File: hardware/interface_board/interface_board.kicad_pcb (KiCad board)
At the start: 2 copper layers, 394.2 x 72.6 mm, 15 parts, among them J1 Conn_01x18_Socket, J10 Conn_01x18_Socket, J2 Conn_01x18_Socket, J3 Conn_01x18_Socket, J4 Conn_01x18_Socket, J5 Conn_01x18_Socket, J6 Conn_01x18_Socket, J7 Conn_01x18_Socket, J8 Conn_01x18_Socket, J9 Conn_01x18_Socket

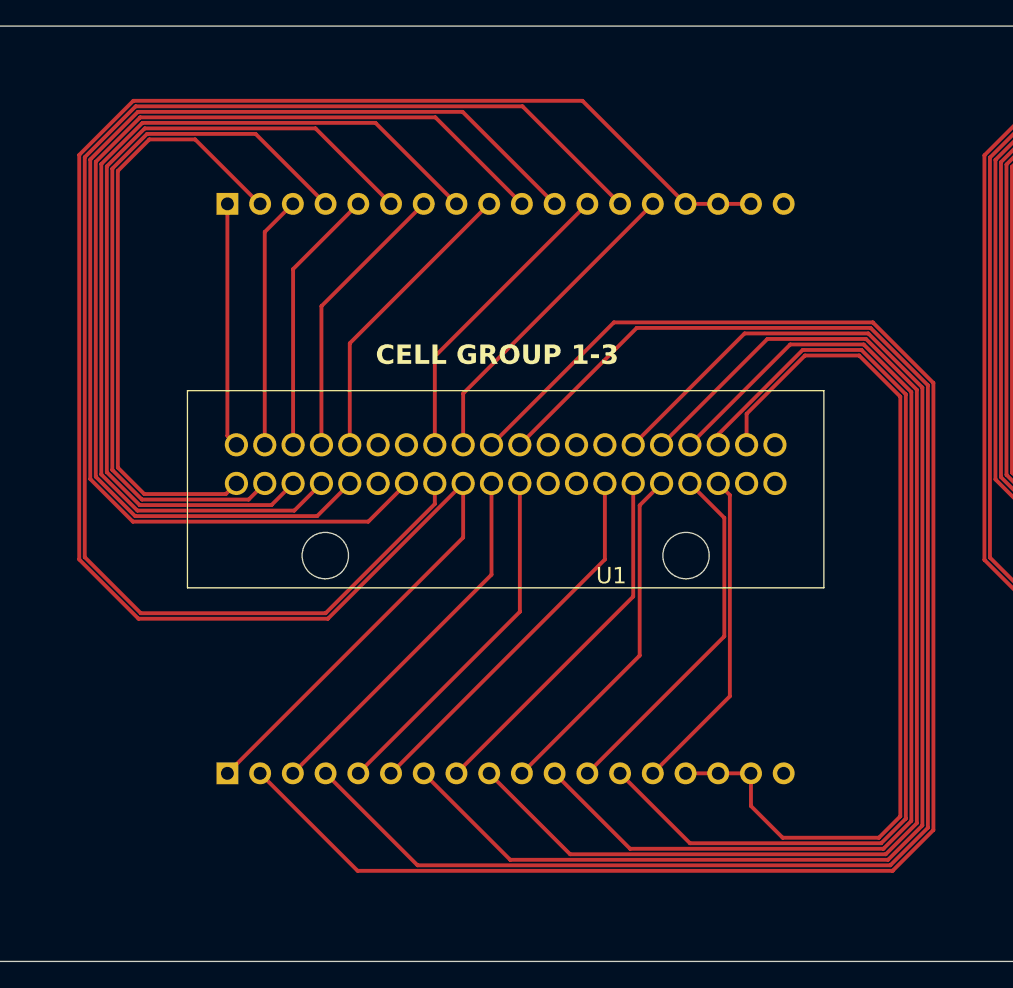
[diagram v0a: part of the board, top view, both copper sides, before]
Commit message: fixed a single connector
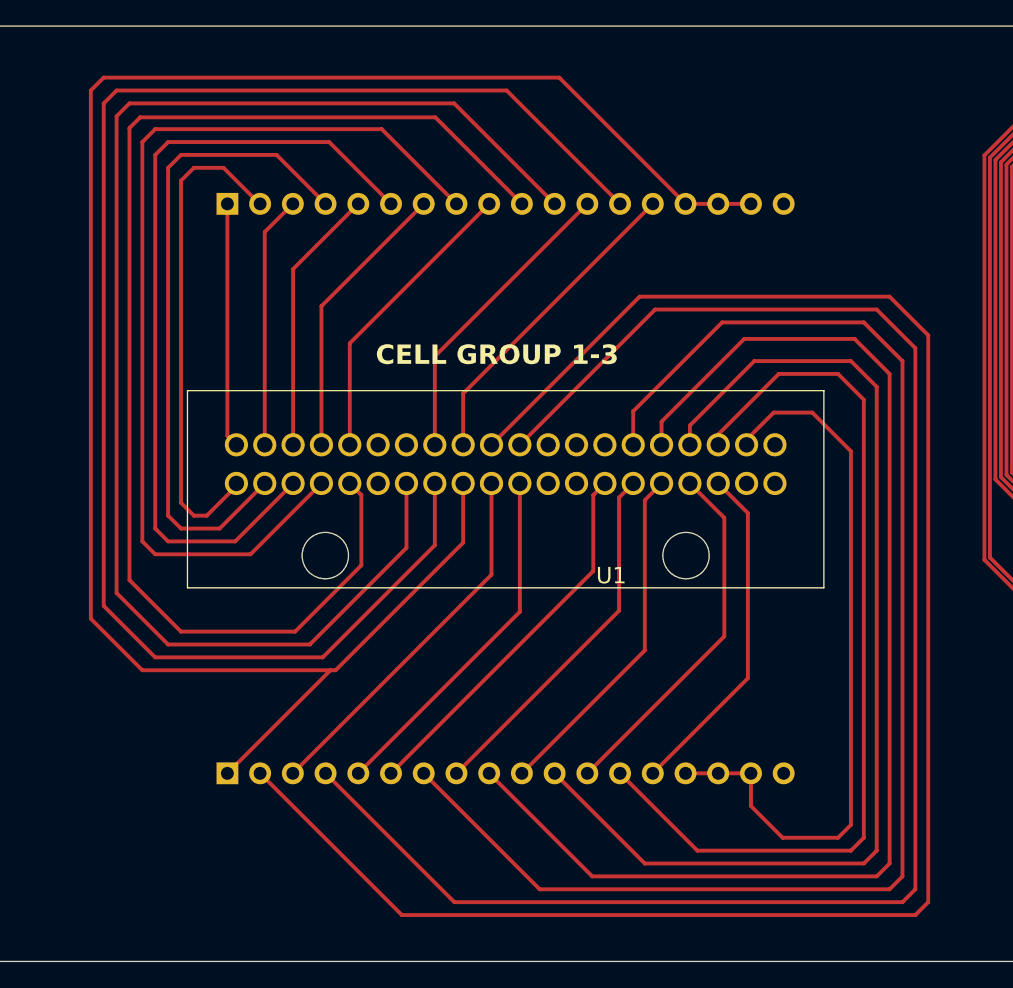
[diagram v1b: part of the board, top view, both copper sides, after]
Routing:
- net 33: track 71.0 -> 56.4 mm
- net -13: track 92.5 -> 106.9 mm
- net 9: track 83.8 -> 97.2 mm
- net 17: track 131.6 -> 140.7 mm
- net 1: track 47.6 -> 38.6 mm
- net 14: track 111.4 -> 118.9 mm
- net 16: track 154.9 -> 147.5 mm
- net 31: track 77.7 -> 70.7 mm
- net 19: track 122.5 -> 128.6 mm
- net 3: track 56.6 -> 50.6 mm
- net 25: track 104.3 -> 108.9 mm
- net 29: track 86.2 -> 83.2 mm
- net 5: track 65.7 -> 62.7 mm
- net 32: track 25.3 -> 26.5 mm
- net 27: track 95.3 -> 96.1 mm

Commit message: Fixed all Connectors
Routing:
- net 105: track 71.0 -> 56.4 mm
- net 177: track 71.0 -> 56.4 mm
- net 141: track 71.0 -> 56.4 mm
- net 69: track 71.0 -> 56.4 mm
- net -85: track 92.5 -> 106.9 mm
- net -157: track 92.5 -> 106.9 mm
- net -49: track 92.5 -> 106.9 mm
- net -121: track 92.5 -> 106.9 mm
- net 81: track 83.8 -> 97.2 mm
- net 45: track 83.8 -> 97.2 mm
- net 153: track 83.8 -> 97.2 mm
- net 117: track 83.8 -> 97.2 mm
- net 89: track 131.6 -> 140.7 mm
- net 125: track 131.6 -> 140.7 mm
- net 53: track 131.6 -> 140.7 mm
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
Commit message: zip tie slots
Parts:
- added H101: MountingHole, MountingHole:MountingHole_3.2mm_M3, F.Cu at (109.9, 107.2)
- added H102: MountingHole, MountingHole:MountingHole_3.2mm_M3, F.Cu at (110.7, 162.2)
- added H103: MountingHole, MountingHole:MountingHole_3.2mm_M3, F.Cu at (336.3, 114.3)
- added H104: MountingHole, MountingHole:MountingHole_3.2mm_M3, F.Cu at (486.9, 112.5)

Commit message: clean up
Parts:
- added H1: MountingHole, MountingHole:MountingHole_3.2mm_M3, F.Cu at (488.3, 166.6)
- moved H103 8.35 mm to (337.0, 106.0)
- moved H104 6.59 mm to (488.2, 106.0)
- moved H102 6.40 mm to (106.0, 166.6)
- moved H101 4.06 mm to (106.0, 106.0)
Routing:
- net 153: track 97.2 -> 86.9 mm
- net 9: track 97.2 -> 86.9 mm
- net 81: track 97.2 -> 86.9 mm
- net 45: track 97.2 -> 86.9 mm
- net 117: track 97.2 -> 86.9 mm
- net 177: track 56.4 -> 59.8 mm
- net 105: track 56.4 -> 59.8 mm
- net 69: track 56.4 -> 59.8 mm
- net 33: track 56.4 -> 59.8 mm
- net 141: track 56.4 -> 59.8 mm
- net 89: track 140.7 -> 139.9 mm
- net 125: track 140.7 -> 139.9 mm
- net 97: track 108.9 -> 108.1 mm
- net 61: track 108.9 -> 108.1 mm
- net 55: track 128.6 -> 127.8 mm
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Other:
- board text added: "Interface Board github.com/Gregification/BeeMS/ 1/20/26 - Uses Orion connectors for E25 - 28 cells per cell group - 14 cells per voltage tap"
